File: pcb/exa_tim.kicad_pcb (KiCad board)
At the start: 4 copper layers, 42 x 42 mm, 51 parts, among them J1 20021112-00010T4LF, J2 FH12-24S-0.5SH(55), Q1 SI2333DS-T1-E3, Q2 DMN3067LW-7, SW1 TL3305CF260QG, SW2 TL3305CF260QG, SW3 TL3305CF260QG, SW4 TL3305CF260QG, U1 STM32L071KZUx, U2 CAM-M8C-0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

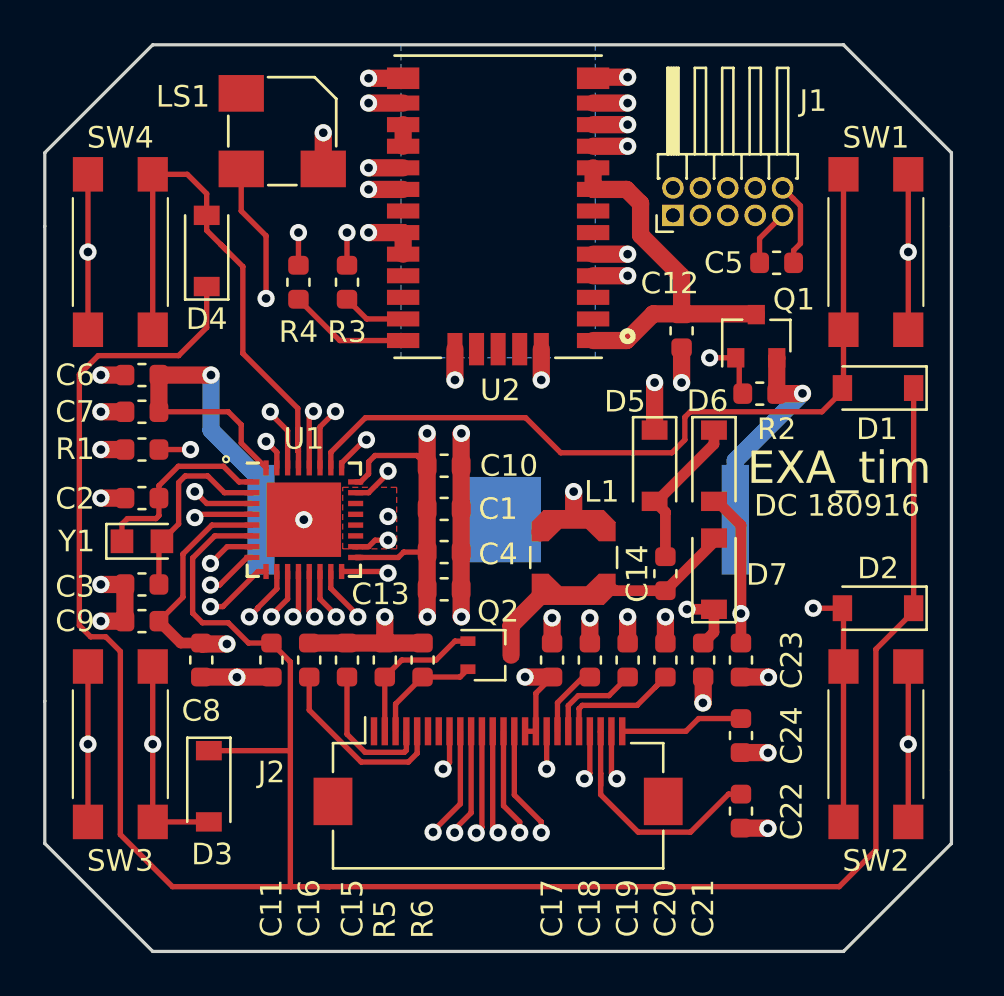
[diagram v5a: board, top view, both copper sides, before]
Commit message: Chang GNSS MOSFET to enh. N-Channel
Changed the MOSFET so that we don't need a pullup,
which might draw some precious power we don't want to
waste.

Also simplifies the BOM.
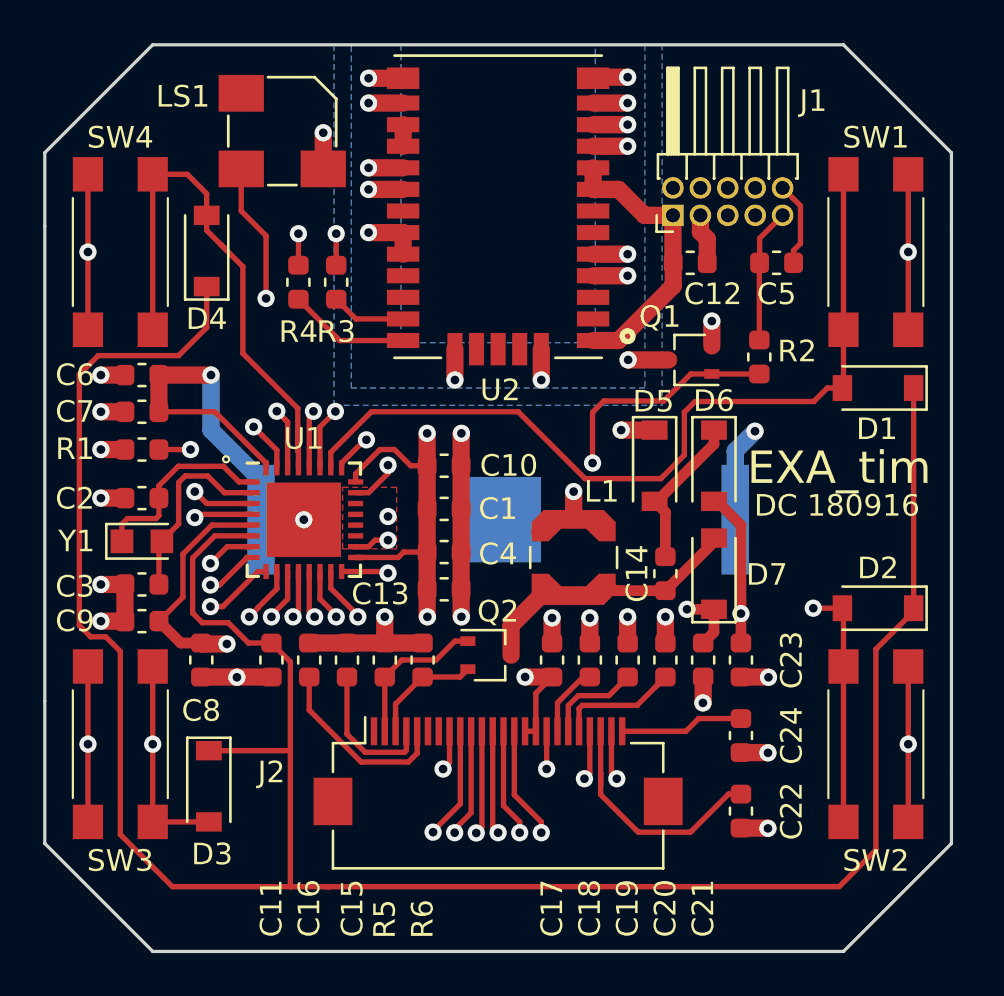
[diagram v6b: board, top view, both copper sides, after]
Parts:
- Q1: value SI2333DS-T1-E3 -> DMN3067LW-7; footprint Package_TO_SOT_SMD:SOT-23 -> Package_TO_SOT_SMD:SOT-323_SC-70
- moved Q1 3.25 mm to (129.9, 84.6), turned to 180 degrees
- moved C12 3.18 mm to (129.9, 80.1), turned to 180 degrees
- moved R2 1.70 mm to (133.1, 84.5), turned to 90 degrees
- moved R3 0.50 mm to (113.5, 81.0)
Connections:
- C12 pad 2: /GNSS_VDD -> 3V
- Q1 pad 2: 3V -> GND
- Q1 pad 3: /GNSS_VDD -> /GNSS_GND
- R2 pad 2: 3V -> GND
- U2 pad 1: /GNSS_VDD -> 3V
- U2 pad 10: GND -> /GNSS_GND
- U2 pad 11: GND -> /GNSS_GND
- U2 pad 12: GND -> /GNSS_GND
- U2 pad 13: GND -> /GNSS_GND
- U2 pad 14: GND -> /GNSS_GND
- U2 pad 15: GND -> /GNSS_GND
- U2 pad 18: GND -> /GNSS_GND
- U2 pad 19: GND -> /GNSS_GND
- U2 pad 21: GND -> /GNSS_GND
- U2 pad 22: GND -> /GNSS_GND
- U2 pad 27: GND -> /GNSS_GND
- U2 pad 31: GND -> /GNSS_GND
- U2 pad 4: GND -> /GNSS_GND
- U2 pad 5: GND -> /GNSS_GND
- U2 pad 8: /GNSS_VDD -> 3V
- U2 pad 9: /GNSS_VDD -> 3V
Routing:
- net /GNSS_EN: track 64.6 -> 33.8 mm
- net /GNSS_GND: track 0.00 -> 23.4 mm, vias 0 -> 14
- net /GNSS_VDD: track 17.5 -> 0.00 mm
- net GND: track 82.4 -> 66.3 mm, vias 41 -> 28
- net 3V: track 95.4 -> 102.9 mm
- net /BTN1: track 38.3 -> 40.1 mm
- net /RX: track 30.5 -> 29.9 mm
- net /TX_GNSS: track 2.98 -> 3.48 mm
- added copper zone on B.Cu, net /GNSS_GND

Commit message: First pass to re-arange parts to move connector
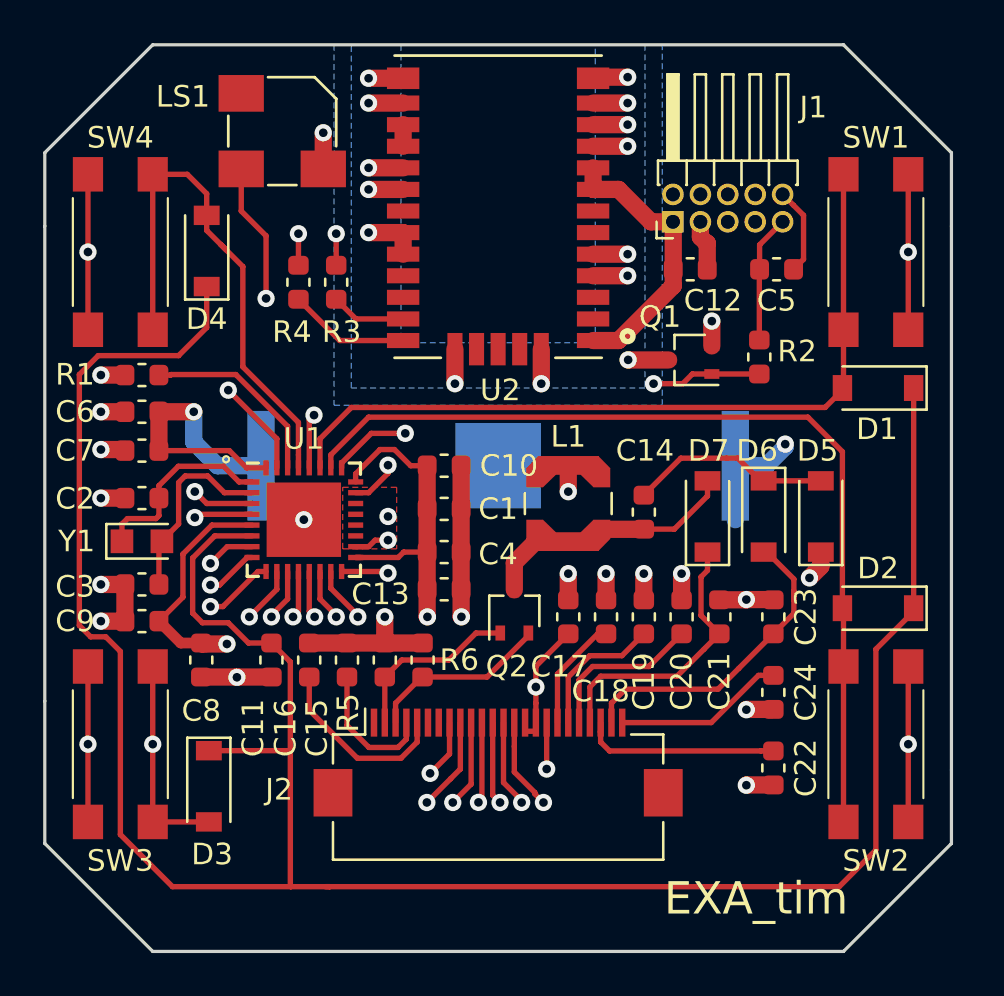
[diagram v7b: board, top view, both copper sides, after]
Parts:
- moved D5 8.05 mm to (135.9, 91.8), turned to 90 degrees
- moved R1 3.45 mm to (104.5, 85.3)
- moved D6 3.29 mm to (133.3, 91.8)
- moved C14 3.02 mm to (127.8, 91.7)
- moved D7 2.67 mm to (130.7, 91.8)
- moved L1 2.51 mm to (124.2, 91.2)
- moved BT1 2.50 mm to (121.0, 89.5)
- moved C22 2.50 mm to (133.8, 103.5)
- moved C23 2.50 mm to (133.8, 96.5), turned to 90 degrees
- moved C24 2.50 mm to (133.8, 100.0)
- moved Q2 2.33 mm to (121.8, 96.2), turned to 90 degrees
- moved C17 2.14 mm to (124.2, 96.5)
- moved C18 2.14 mm to (126.0, 96.5)
- moved C19 2.14 mm to (127.8, 96.5)
- moved C20 2.14 mm to (129.5, 96.5)
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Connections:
- U1 pad 26: /BTN1 -> /BTN2
- U1 pad 27: /BTN2 -> /BTN1
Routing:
- net 3V: track 102.9 -> 96.1 mm, vias 11 -> 10
- net /PREVGL: track 20.5 -> 15.0 mm, vias 2 -> 0
- net /RESE: track 5.28 -> 8.47 mm
- net /BTN1: track 40.1 -> 37.3 mm
- net /PREVGH: track 15.7 -> 13.0 mm, vias 2 -> 0
- net Net-(C22-Pad1): track 11.5 -> 9.11 mm
- net /BUSY: track 24.6 -> 22.2 mm
- net /CS: track 22.8 -> 20.5 mm
- net Net-(C18-Pad1): track 3.32 -> 5.58 mm
- net Net-(C24-Pad1): track 5.74 -> 7.91 mm
- net Net-(C14-Pad1): track 7.27 -> 9.34 mm
- net Net-(C19-Pad1): track 4.55 -> 6.50 mm
- net /NRST: track 45.7 -> 47.4 mm
- net /RESET: track 21.4 -> 19.8 mm
- net GND: track 66.3 -> 67.9 mm, vias 28 -> 26
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
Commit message: Switched backt to high side p-channel MOSFET
I don't want to risk communication errros of UART
because of the otherwise not common ground levels.
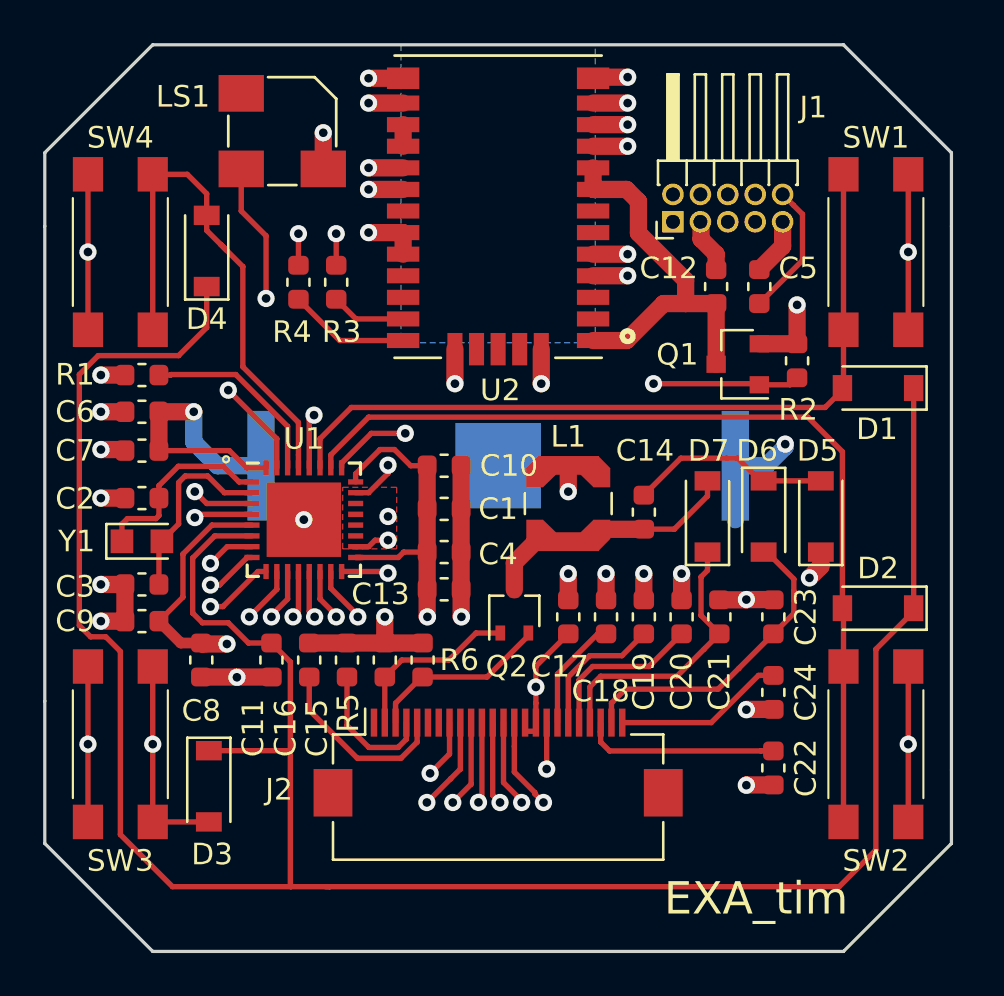
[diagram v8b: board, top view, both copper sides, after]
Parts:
- C2, C3: value 20pF -> 4pF
- Q1: value DMN3067LW-7 -> SI2333DS-T1-E3; footprint Package_TO_SOT_SMD:SOT-323_SC-70 -> Package_TO_SOT_SMD:SOT-23
- Y1: value 9HT11-32.768KDZF-T -> 9HT11-32.768KDZB-T
- moved Q1 2.21 mm to (132.1, 84.8)
- moved R2 1.76 mm to (134.8, 84.6)
- moved C12 1.44 mm to (131.1, 81.2), turned to 270 degrees
- moved C5 1.13 mm to (133.1, 81.2), turned to 270 degrees
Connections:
- C12 pad 2: 3V -> /VDD_GNSS
- Q1 pad 2: GND -> 3V
- Q1 pad 3: /GNSS_GND -> /VDD_GNSS
- R2 pad 2: GND -> 3V
- U2 pad 1: 3V -> /VDD_GNSS
- U2 pad 10: /GNSS_GND -> GND
- U2 pad 11: /GNSS_GND -> GND
- U2 pad 12: /GNSS_GND -> GND
- U2 pad 13: /GNSS_GND -> GND
- U2 pad 14: /GNSS_GND -> GND
- U2 pad 15: /GNSS_GND -> GND
- U2 pad 18: /GNSS_GND -> GND
- U2 pad 19: /GNSS_GND -> GND
- U2 pad 21: /GNSS_GND -> GND
- U2 pad 22: /GNSS_GND -> GND
- U2 pad 27: /GNSS_GND -> GND
- U2 pad 31: /GNSS_GND -> GND
- U2 pad 4: /GNSS_GND -> GND
- U2 pad 5: /GNSS_GND -> GND
- U2 pad 8: 3V -> /VDD_GNSS
- U2 pad 9: 3V -> /VDD_GNSS
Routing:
- net /GNSS_GND: track 23.7 -> 0.00 mm, vias 14 -> 0
- net /VDD_GNSS: track 0.00 -> 18.2 mm
- net GND: track 67.9 -> 85.5 mm, vias 26 -> 38
- net 3V: track 96.1 -> 86.6 mm, vias 10 -> 11
- net /NRST: track 47.4 -> 49.6 mm
- net /GNSS_EN: track 32.5 -> 34.1 mm
- removed copper zone on B.Cu, net /GNSS_GND
